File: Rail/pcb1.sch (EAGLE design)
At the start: 45 parts, among them J6 638207222005, J7 638207222005, U4 TLE9250VSJ, X1 S4P-VH

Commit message: ..
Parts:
- removed J4, J8: (no value), Wurth_Connectors_WR-PHD:6130XX21121_61300621121
- added J5, J9: (no value), 6-pin-tht:6130XX21121_61300621121
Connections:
- net ECU_GND: now also J9.2, J9.4, J9.6; no longer J4.2, J4.4, J4.6
- net ECU_PWR: now also J5.2, J5.4, J5.6; no longer J8.2, J8.4, J8.6
- net PWR: now also J5.1, J5.3, J5.5; no longer J8.1, J8.3, J8.5
- net PWR_GND: now also J9.1, J9.3, J9.5; no longer J4.1, J4.3, J4.5

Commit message: ..
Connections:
- net +5V: now also J1.2, J1.4
- net ECU_GND: now also J1.1, J1.3
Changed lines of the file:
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@@
 <part name="J5" library="6-pin-tht" deviceset="6130XX21121_61300621121" device="" package3d_urn="urn:adsk.eagle:package:14805407/2"/>
 <part name="J9" library="6-pin-tht" deviceset="6130XX21121_61300621121" device="" package3d_urn="urn:adsk.eagle:package:14805407/2"/>
+<part name="ECU_GND11" library="supply_isobus" deviceset="ECU_GND" device=""/>
+<part name="ECU_GND12" library="supply_isobus" deviceset="ECU_GND" device=""/>
+<part name="P+3" library="supply1" deviceset="+5V" device=""/>
+<part name="P+5" library="supply1" deviceset="+5V" device=""/>
 </parts>
 <sheets>
@@
 </plain>
 <instances>
-<instance part="J1" gate="G$1" x="-20.32" y="116.84" smashed="yes">
-<attribute name="NAME" x="-34.2" y="117.19" size="1.016" layer="95" align="bottom-right"/>
-<attribute name="VALUE" x="-34.06" y="114.97" size="1.016" layer="96" align="bottom-right"/>
-</instance>
 <instance part="J6" gate="G$1" x="-25.4" y="93.98" smashed="yes">
 <attribute name="NAME" x="-25.31" y="95.315" size="1.016" layer="95" align="bottom-right"/>
@@
 <attribute name="VALUE" x="-22.86" y="48.26" size="1.778" layer="96"/>
 </instance>
+<instance part="J1" gate="G$1" x="167.64" y="73.66" smashed="yes">
+<attribute name="NAME" x="153.76" y="74.01" size="1.016" layer="95" align="bottom-right"/>
+<attribute name="VALUE" x="153.9" y="71.79" size="1.016" layer="96" align="bottom-right"/>
+</instance>
+<instance part="ECU_GND11" gate="ECU_GND" x="157.48" y="58.42" smashed="yes">
+<attribute name="VALUE" x="154.94" y="55.88" size="1.778" layer="96"/>
+</instance>
+<instance part="ECU_GND12" gate="ECU_GND" x="160.02" y="60.96" smashed="yes">
+<attribute name="VALUE" x="157.48" y="58.42" size="1.778" layer="96"/>
+</instance>
+<instance part="P+3" gate="1" x="160.02" y="88.9" smashed="yes" rot="MR0">
+<attribute name="VALUE" x="162.56" y="83.82" size="1.778" layer="96" rot="MR90"/>
+</instance>
+<instance part="P+5" gate="1" x="157.48" y="96.52" smashed="yes" rot="MR0">
+<attribute name="VALUE" x="160.02" y="91.44" size="1.778" layer="96" rot="MR90"/>
+</instance>
 </instances>
 <busses>
@@
 <wire x1="66.04" y1="83.82" x2="66.04" y2="68.58" width="0.1524" layer="91"/>
 <junction x="53.34" y="83.82"/>
+</segment>
+<segment>
+<pinref part="J1" gate="G$1" pin="4"/>
+<pinref part="P+3" gate="1" pin="+5V"/>
+<wire x1="160.02" y1="86.36" x2="160.02" y2="78.74" width="0.1524" layer="91"/>
+</segment>
+<segment>
+<pinref part="J1" gate="G$1" pin="2"/>
+<pinref part="P+5" gate="1" pin="+5V"/>
+<wire x1="157.48" y1="93.98" x2="157.48" y2="78.74" width="0.1524" layer="91"/>
 </segment>
 </net>
@@
 <pinref part="GND2" gate="1" pin="GND"/>
 </segment>
-</net>
+<segment>
+<pinref part="J1" gate="G$1" pin="1"/>
+<pinref part="ECU_GND11" gate="ECU_GND" pin="ECU_GND"/>
+<wire x1="157.48" y1="60.96" x2="157.48" y2="68.58" width="0.1524" layer="91"/>
+</segment>
+<segment>
+<pinref part="J1" gate="G$1" pin="3"/>
+<pinref part="ECU_GND12" gate="ECU_GND" pin="ECU_GND"/>
+<wire x1="160.02" y1="63.5" x2="160.02" y2="68.58" width="0.1524" layer="91"/>
+</segment>
+</net>

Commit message: should be OK so far... ask Schillinger about the LED Cooling.
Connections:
- net +3V3: now also J1.2
- net +5V: now also J1.3; no longer J1.2, J1.4
- net ECU_GND: no longer J1.3
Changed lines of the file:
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@@
 <part name="J9" library="6-pin-tht" deviceset="6130XX21121_61300621121" device="" package3d_urn="urn:adsk.eagle:package:14805407/2"/>
 <part name="ECU_GND11" library="supply_isobus" deviceset="ECU_GND" device=""/>
-<part name="ECU_GND12" library="supply_isobus" deviceset="ECU_GND" device=""/>
 <part name="P+3" library="supply1" deviceset="+5V" device=""/>
-<part name="P+5" library="supply1" deviceset="+5V" device=""/>
+<part name="+3V3" library="supply1" deviceset="+3V3" device=""/>
 </parts>
 <sheets>
@@
 <attribute name="VALUE" x="154.94" y="55.88" size="1.778" layer="96"/>
 </instance>
-<instance part="ECU_GND12" gate="ECU_GND" x="160.02" y="60.96" smashed="yes">
-<attribute name="VALUE" x="157.48" y="58.42" size="1.778" layer="96"/>
-</instance>
-<instance part="P+3" gate="1" x="160.02" y="88.9" smashed="yes" rot="MR0">
-<attribute name="VALUE" x="162.56" y="83.82" size="1.778" layer="96" rot="MR90"/>
-</instance>
-<instance part="P+5" gate="1" x="157.48" y="96.52" smashed="yes" rot="MR0">
-<attribute name="VALUE" x="160.02" y="91.44" size="1.778" layer="96" rot="MR90"/>
+<instance part="P+3" gate="1" x="160.02" y="43.18" smashed="yes" rot="MR180">
+<attribute name="VALUE" x="157.48" y="48.26" size="1.778" layer="96" rot="MR270"/>
+</instance>
+<instance part="+3V3" gate="G$1" x="157.48" y="83.82" smashed="yes">
+<attribute name="VALUE" x="154.305" y="85.09" size="1.778" layer="96"/>
 </instance>
 </instances>
@@
 </segment>
 <segment>
-<pinref part="J1" gate="G$1" pin="4"/>
+<pinref part="J1" gate="G$1" pin="3"/>
+<wire x1="160.02" y1="68.58" x2="160.02" y2="45.72" width="0.1524" layer="91"/>
 <pinref part="P+3" gate="1" pin="+5V"/>
-<wire x1="160.02" y1="86.36" x2="160.02" y2="78.74" width="0.1524" layer="91"/>
-</segment>
-<segment>
-<pinref part="J1" gate="G$1" pin="2"/>
-<pinref part="P+5" gate="1" pin="+5V"/>
-<wire x1="157.48" y1="93.98" x2="157.48" y2="78.74" width="0.1524" layer="91"/>
 </segment>
 </net>
@@
 <wire x1="157.48" y1="60.96" x2="157.48" y2="68.58" width="0.1524" layer="91"/>
 </segment>
-<segment>
-<pinref part="J1" gate="G$1" pin="3"/>
-<pinref part="ECU_GND12" gate="ECU_GND" pin="ECU_GND"/>
-<wire x1="160.02" y1="63.5" x2="160.02" y2="68.58" width="0.1524" layer="91"/>
-</segment>
-</net>
+</net>
+<net name="+3V3" class="0">
+<segment>
+<pinref part="+3V3" gate="G$1" pin="+3V3"/>
+<wire x1="157.48" y1="78.74" x2="157.48" y2="81.28" width="0.1524" layer="91"/>
+<pinref part="J1" gate="G$1" pin="2"/>
+</segment>
+</net>

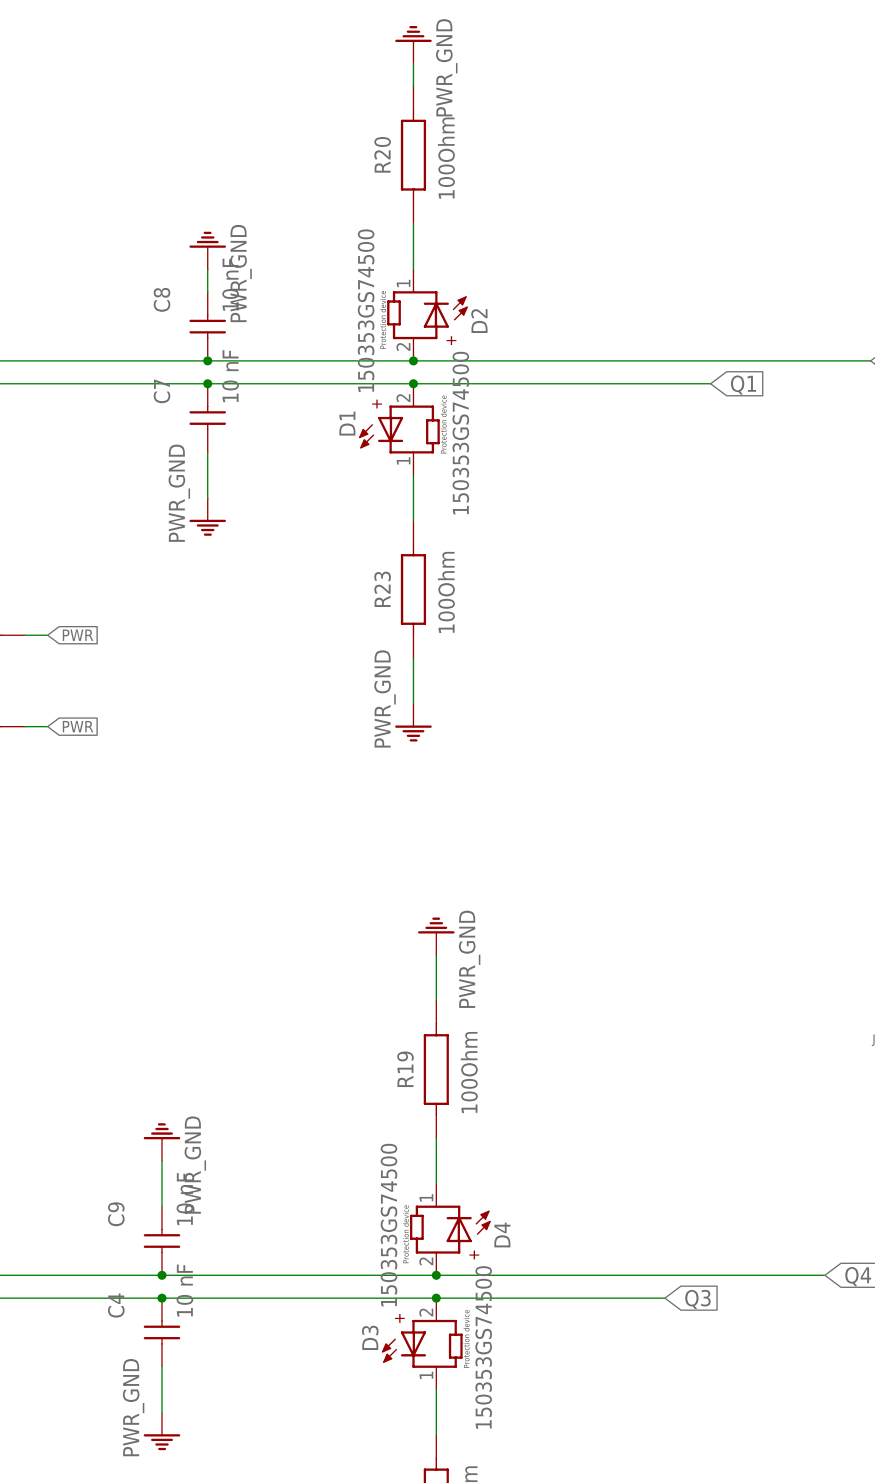
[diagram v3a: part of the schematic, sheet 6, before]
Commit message: Cooling of LED !
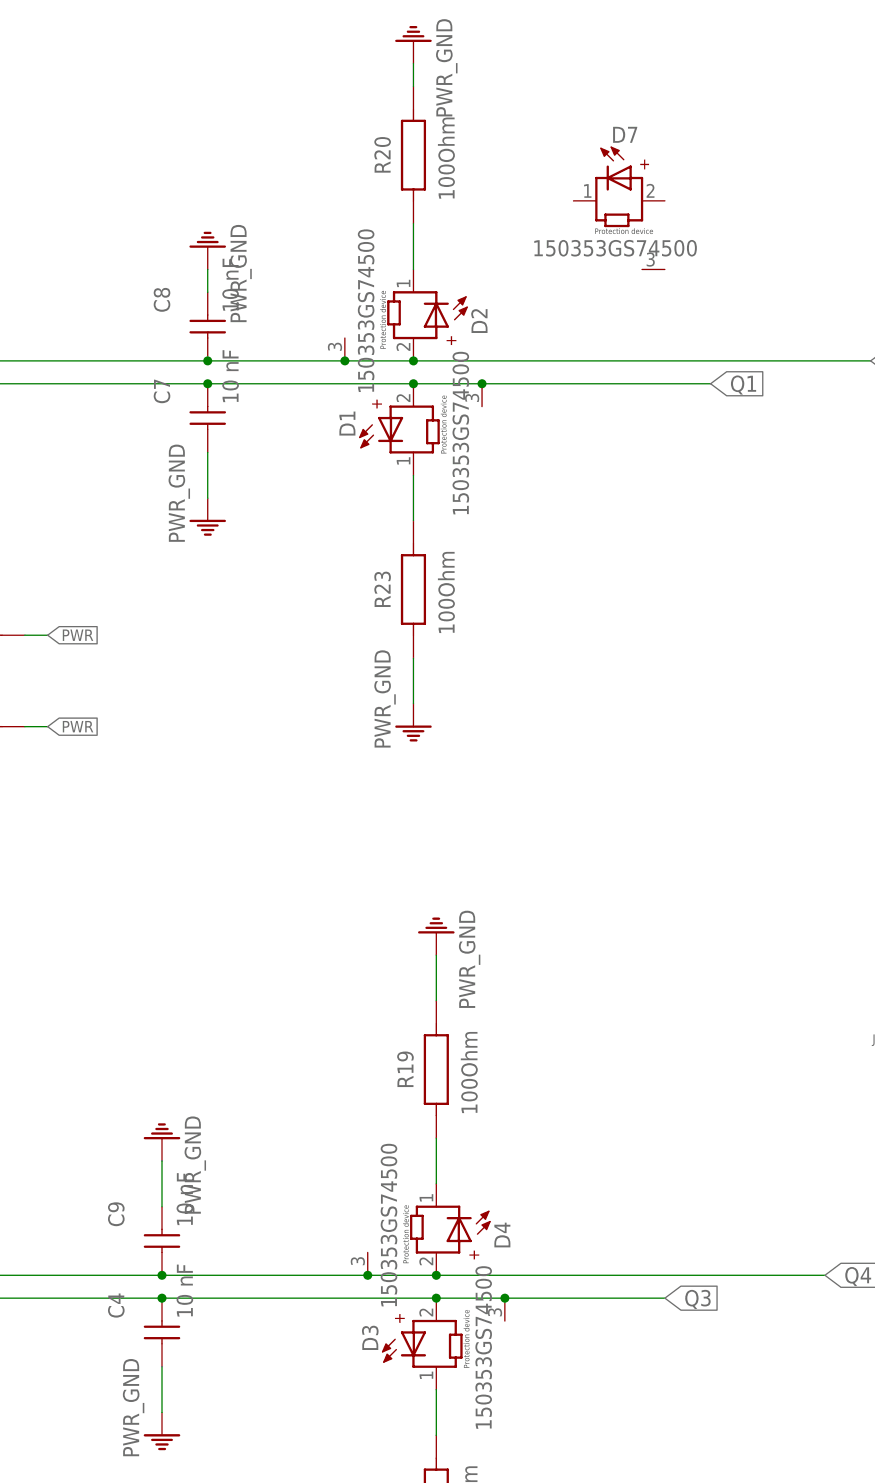
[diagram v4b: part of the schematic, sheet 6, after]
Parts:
- added D7: 150353GS74500, LED:WL-SMDC_3535_150353GS74500
- D1, D2, D3, D4: device Wurth_LEDs_WL-SMDC:WL-SMDC_3535_150353GS74500 -> LED:WL-SMDC_3535_150353GS74500
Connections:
- net Q1: now also D1.COOL
- net Q2: now also D2.COOL
- net Q3: now also D3.COOL
- net Q4: now also D4.COOL
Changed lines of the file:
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@@
 <part name="C12" library="Wurth_Capacitors_WCAP-CSGP" library_urn="urn:adsk.eagle:library:18488985" deviceset="WCAP-CSGP_0805_H1.25" device="_10V(DC)" package3d_urn="urn:adsk.eagle:package:18489127/2" technology="_885012107011" value="22  µF "/>
 <part name="D0" library="Wurth_EMC Components_WE-TVSP" library_urn="urn:adsk.eagle:library:14283044" deviceset="WE-TVSP_DO-214AB_3000W_BI" device="" package3d_urn="urn:adsk.eagle:package:12146529/2" technology="_824551331" value="33V"/>
-<part name="D2" library="Wurth_LEDs_WL-SMDC" library_urn="urn:adsk.eagle:library:19063442" deviceset="WL-SMDC_3535" device="" package3d_urn="urn:adsk.eagle:package:19063445/2" technology="_150353GS74500" value="150353GS74500"/>
-<part name="D1" library="Wurth_LEDs_WL-SMDC" library_urn="urn:adsk.eagle:library:19063442" deviceset="WL-SMDC_3535" device="" package3d_urn="urn:adsk.eagle:package:19063445/2" technology="_150353GS74500" value="150353GS74500"/>
-<part name="D4" library="Wurth_LEDs_WL-SMDC" library_urn="urn:adsk.eagle:library:19063442" deviceset="WL-SMDC_3535" device="" package3d_urn="urn:adsk.eagle:package:19063445/2" technology="_150353GS74500" value="150353GS74500"/>
-<part name="D3" library="Wurth_LEDs_WL-SMDC" library_urn="urn:adsk.eagle:library:19063442" deviceset="WL-SMDC_3535" device="" package3d_urn="urn:adsk.eagle:package:19063445/2" technology="_150353GS74500" value="150353GS74500"/>
+<part name="D2" library="LED" deviceset="WL-SMDC_3535" device="" package3d_urn="urn:adsk.eagle:package:19063445/2" technology="_150353GS74500" value="150353GS74500"/>
+<part name="D1" library="LED" deviceset="WL-SMDC_3535" device="" package3d_urn="urn:adsk.eagle:package:19063445/2" technology="_150353GS74500" value="150353GS74500"/>
+<part name="D4" library="LED" deviceset="WL-SMDC_3535" device="" package3d_urn="urn:adsk.eagle:package:19063445/2" technology="_150353GS74500" value="150353GS74500"/>
+<part name="D3" library="LED" deviceset="WL-SMDC_3535" device="" package3d_urn="urn:adsk.eagle:package:19063445/2" technology="_150353GS74500" value="150353GS74500"/>
 <part name="R19" library="Wurth_Resistor_WRIS-KWKB" library_urn="urn:adsk.eagle:library:13351500" deviceset="WRIS-KWKB_0612" device="" package3d_urn="urn:adsk.eagle:package:13351506/2" technology="_561020132008" value="100Ohm"/>
 <part name="R20" library="Wurth_Resistor_WRIS-KWKB" library_urn="urn:adsk.eagle:library:13351500" deviceset="WRIS-KWKB_0612" device="" package3d_urn="urn:adsk.eagle:package:13351506/2" technology="_561020132008" value="100Ohm"/>
@@
 <part name="P+3" library="supply1" deviceset="+5V" device=""/>
 <part name="+3V3" library="supply1" deviceset="+3V3" device=""/>
+<part name="D7" library="LED" deviceset="WL-SMDC_3535" device="" package3d_urn="urn:adsk.eagle:package:19063445/2" technology="_150353GS74500" value="150353GS74500"/>
 </parts>
 <sheets>
@@
 <attribute name="VALUE" x="247.88" y="43.85" size="1.016" layer="96" align="bottom-right"/>
 </instance>
+<instance part="D7" gate="G$1" x="180.34" y="139.7" smashed="yes">
+<attribute name="NAME" x="180.99" y="146.15" size="1.778" layer="95" align="bottom-center"/>
+<attribute name="VALUE" x="179.89" y="133.55" size="1.778" layer="96" align="bottom-center"/>
+</instance>
 </instances>
 <busses>
@@
 <label x="203.2" y="20.32" size="1.778" layer="95" xref="yes"/>
 <pinref part="D4" gate="G$1" pin="+"/>
-<wire x1="160.02" y1="20.32" x2="129.54" y2="20.32" width="0.1524" layer="91"/>
+<wire x1="160.02" y1="20.32" x2="152.4" y2="20.32" width="0.1524" layer="91"/>
 <junction x="160.02" y="20.32"/>
+<pinref part="D4" gate="G$1" pin="COOL"/>
+<junction x="152.4" y="20.32"/>
+<wire x1="152.4" y1="20.32" x2="129.54" y2="20.32" width="0.1524" layer="91"/>
 </segment>
 </net>
@@
 <pinref part="C4" gate="G$1" pin="2"/>
 <junction x="129.54" y="17.78"/>
-<wire x1="185.42" y1="17.78" x2="160.02" y2="17.78" width="0.1524" layer="91"/>
+<wire x1="185.42" y1="17.78" x2="167.64" y2="17.78" width="0.1524" layer="91"/>
 <label x="185.42" y="17.78" size="1.778" layer="95" xref="yes"/>
 <pinref part="D3" gate="G$1" pin="+"/>
+<wire x1="167.64" y1="17.78" x2="160.02" y2="17.78" width="0.1524" layer="91"/>
 <wire x1="160.02" y1="17.78" x2="129.54" y2="17.78" width="0.1524" layer="91"/>
 <junction x="160.02" y="17.78"/>
+<pinref part="D3" gate="G$1" pin="COOL"/>
+<junction x="167.64" y="17.78"/>
 </segment>
 </net>
@@
 <label x="208.28" y="121.92" size="1.778" layer="95" xref="yes"/>
 <pinref part="D2" gate="G$1" pin="+"/>
-<wire x1="157.48" y1="121.92" x2="134.62" y2="121.92" width="0.1524" layer="91"/>
+<wire x1="157.48" y1="121.92" x2="149.86" y2="121.92" width="0.1524" layer="91"/>
 <junction x="157.48" y="121.92"/>
+<pinref part="D2" gate="G$1" pin="COOL"/>
+<junction x="149.86" y="121.92"/>
+<wire x1="149.86" y1="121.92" x2="134.62" y2="121.92" width="0.1524" layer="91"/>
 </segment>
 </net>
@@
 <pinref part="C7" gate="G$1" pin="2"/>
 <junction x="134.62" y="119.38"/>
-<wire x1="190.5" y1="119.38" x2="157.48" y2="119.38" width="0.1524" layer="91"/>
+<wire x1="190.5" y1="119.38" x2="165.1" y2="119.38" width="0.1524" layer="91"/>
 <label x="190.5" y="119.38" size="1.778" layer="95" xref="yes"/>
 <pinref part="D1" gate="G$1" pin="+"/>
+<wire x1="165.1" y1="119.38" x2="157.48" y2="119.38" width="0.1524" layer="91"/>
 <wire x1="157.48" y1="119.38" x2="134.62" y2="119.38" width="0.1524" layer="91"/>
 <junction x="157.48" y="119.38"/>
-</segment>
-</net>
+<pinref part="D1" gate="G$1" pin="COOL"/>
+<junction x="165.1" y="119.38"/>
+</segment>
+</net>

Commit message: therm
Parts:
- removed D7: 150353GS74500, LED:WL-SMDC_3535_150353GS74500
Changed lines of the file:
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@@
 <part name="P+3" library="supply1" deviceset="+5V" device=""/>
 <part name="+3V3" library="supply1" deviceset="+3V3" device=""/>
-<part name="D7" library="LED" deviceset="WL-SMDC_3535" device="" package3d_urn="urn:adsk.eagle:package:19063445/2" technology="_150353GS74500" value="150353GS74500"/>
 </parts>
 <sheets>
@@
 <attribute name="VALUE" x="247.88" y="43.85" size="1.016" layer="96" align="bottom-right"/>
 </instance>
-<instance part="D7" gate="G$1" x="180.34" y="139.7" smashed="yes">
-<attribute name="NAME" x="180.99" y="146.15" size="1.778" layer="95" align="bottom-center"/>
-<attribute name="VALUE" x="179.89" y="133.55" size="1.778" layer="96" align="bottom-center"/>
-</instance>
 </instances>
